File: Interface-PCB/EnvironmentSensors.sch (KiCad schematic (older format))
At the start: 10 parts, among them J10 LEVEL_SENSOR, J11 LEVEL_SENSOR, J12 LEVEL_SENSOR, J13 TEMPERATURE_SENSOR, J14 TEMPERATURE_SENSOR, J7 LEVEL_SENSOR, J8 LEVEL_SENSOR, J9 LEVEL_SENSOR

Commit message: Assign misc footprints for FDP
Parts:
- R13, R14: footprint (none) -> Resistors:AXIAL-0.3-KIT
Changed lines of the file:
@@
 F 0 "R13" H 9220 5546 50  0000 L CNN
 F 1 "4.7k" H 9220 5455 50  0000 L CNN
-F 2 "" V 9080 5500 50  0001 C CNN
+F 2 "Resistors:AXIAL-0.3-KIT" V 9080 5500 50  0001 C CNN
 F 3 "~" H 9150 5500 50  0001 C CNN
 	1    9150 5500
@@
 F 0 "R14" H 9180 4446 50  0000 R CNN
 F 1 "10k" H 9180 4355 50  0000 R CNN
-F 2 "" V 9180 4400 50  0001 C CNN
+F 2 "Resistors:AXIAL-0.3-KIT" V 9180 4400 50  0001 C CNN
 F 3 "~" H 9250 4400 50  0001 C CNN
 	1    9250 4400

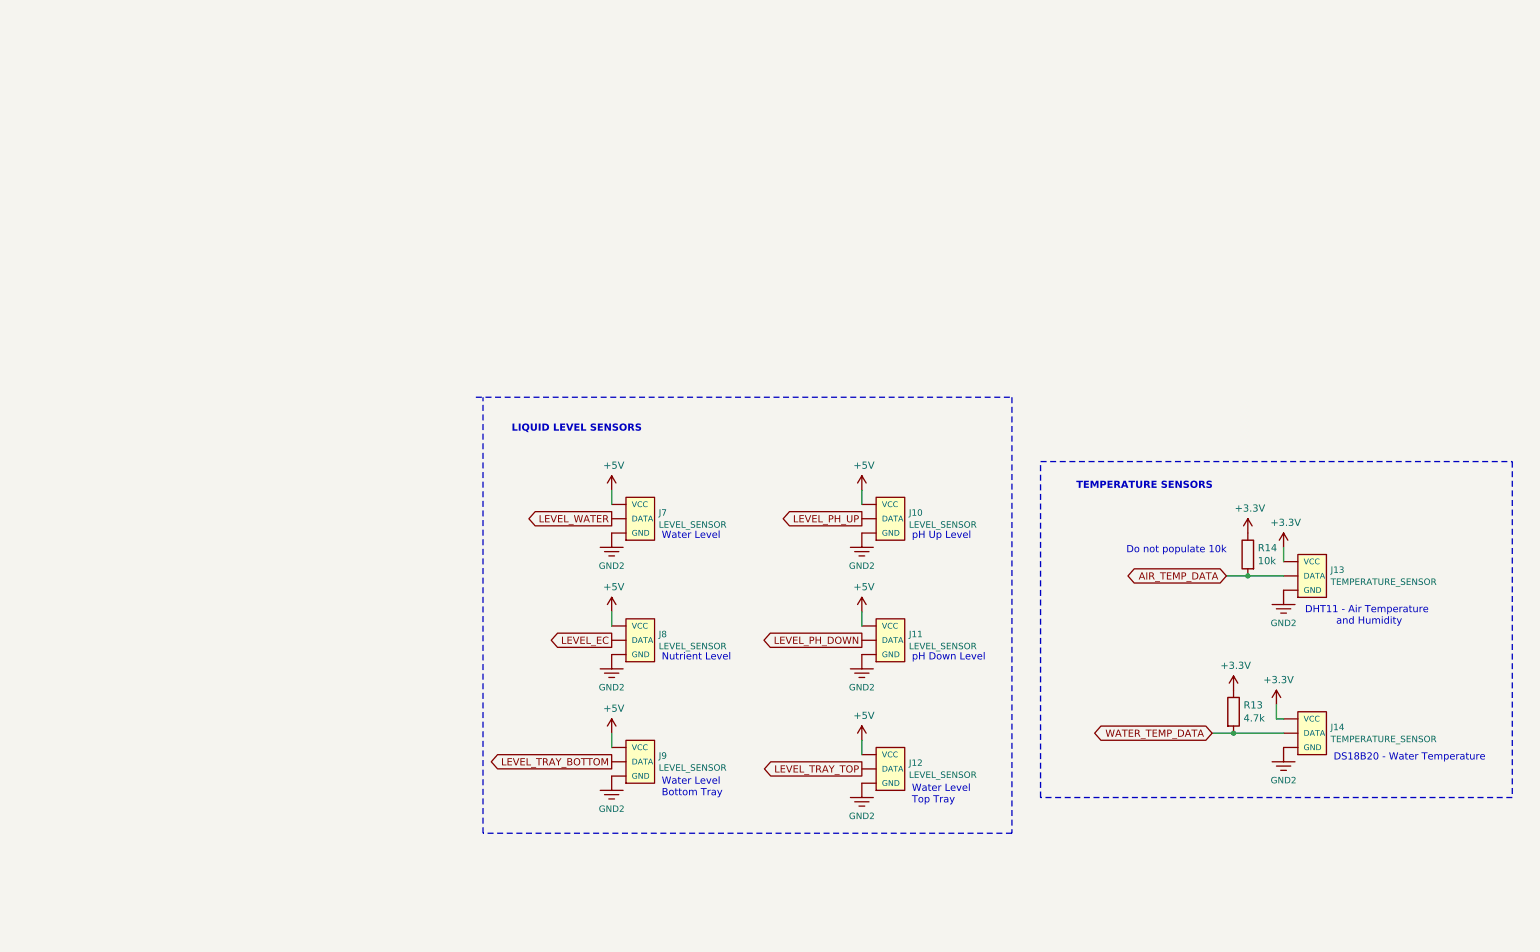
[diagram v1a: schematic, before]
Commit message: Add diagrams and datasheets
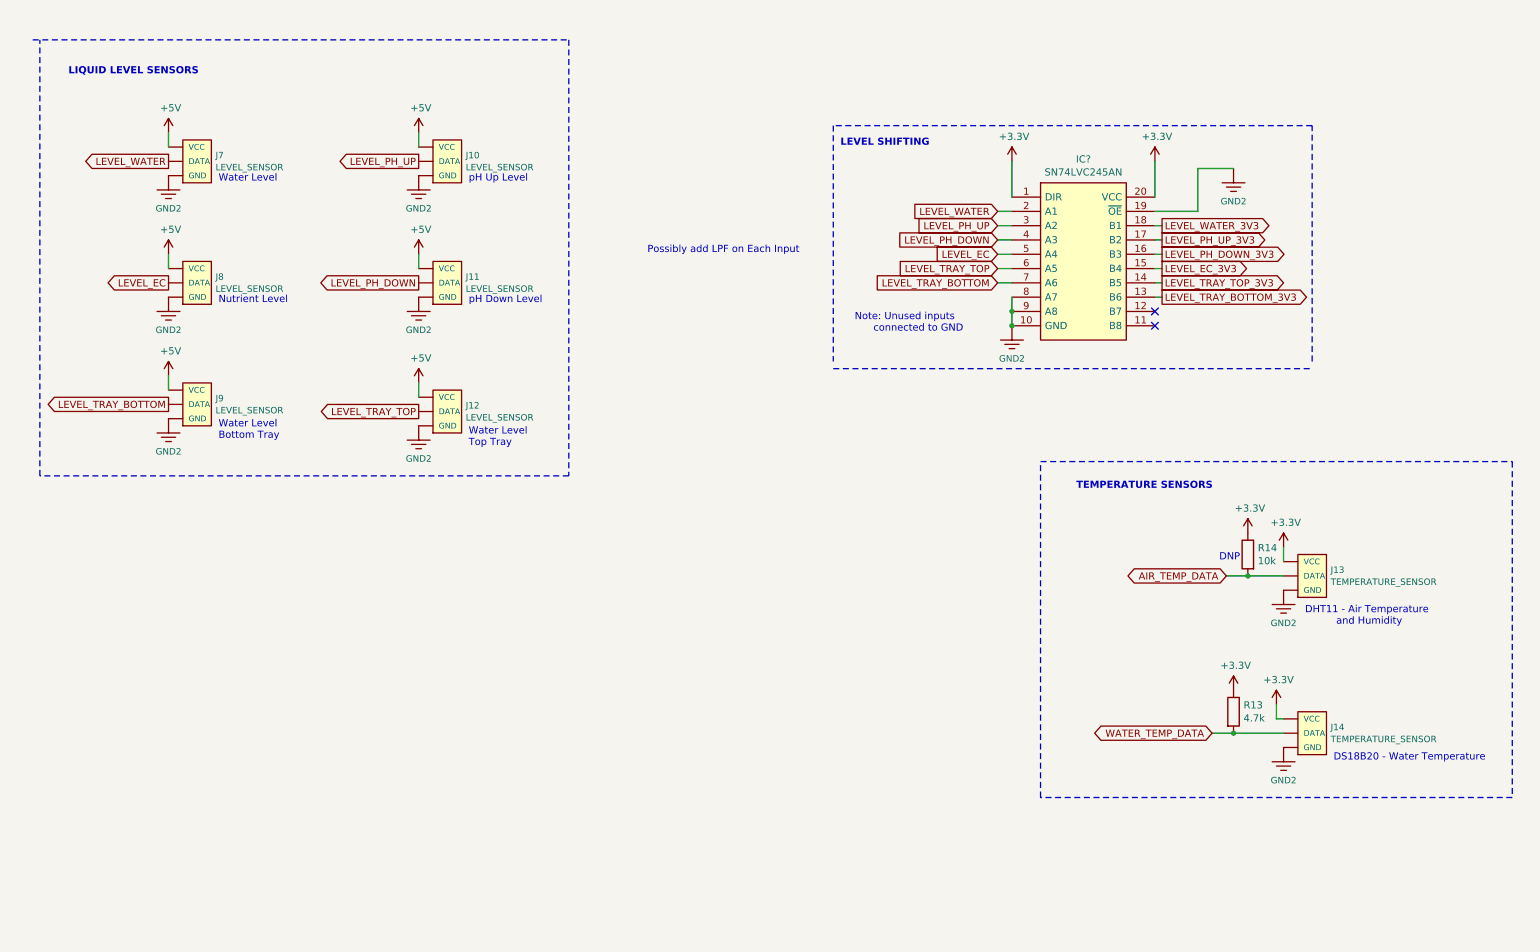
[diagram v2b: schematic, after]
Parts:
- added IC?: SN74LVC245AN, Package_DIP:DIP-20_W7.62mm_LongPads, symbol AA_Custom_Components:SN74LVC245AN
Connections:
- net +3V3: now also IC?.1 (DIR), IC?.20 (VCC)
- net 3.3V: now also IC?.10 (GND), IC?.19 (~OE), IC?.8 (A7), IC?.9 (A8)
- net LEVEL_EC: now also IC?.5 (A4)
- net LEVEL_PH_DOWN: now also IC?.4 (A3)
- net LEVEL_PH_UP: now also IC?.3 (A2)
- net LEVEL_TRAY_BOTTOM: now also IC?.7 (A6)
- net LEVEL_TRAY_TOP: now also IC?.6 (A5)
- net LEVEL_WATER: now also IC?.2 (A1)
- new net LEVEL_EC_3V3: IC?.15 (B4)
- new net LEVEL_PH_DOWN_3V3: IC?.16 (B3)
- new net LEVEL_PH_UP_3V3: IC?.17 (B2)
- new net LEVEL_TRAY_BOTTOM_3V3: IC?.13 (B6)
- new net LEVEL_TRAY_TOP_3V3: IC?.14 (B5)
- new net LEVEL_WATER_3V3: IC?.18 (B1)
- no-connect marks 0 -> 2
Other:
- note added: "DNP"
- note added: "LEVEL SHIFTING"
- note added: "Note: Unused inputs\n connected to GND"
- note added: "Possibly add LPF on Each Input"
- note removed: "Do not populate 10k"
- moved on the sheet: J10, J11, J12, J7, J8, J9

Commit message: Review Schematic
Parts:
- added C3: 100nF, Capacitor_THT:C_Disc_D3.4mm_W2.1mm_P2.50mm, symbol Device:C
- gave numbers to parts that had none: 1
- renumbered J9 to J10, J10 to J11, J11 to J12, J12 to J13, J13 to J14, J14 to J15, J7 to J8, J8 to J9, R13 to R7, R14 to R8
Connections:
- net +3V3: now also C3.1
- net 3.3V renamed GND
- net GND: now also C3.2
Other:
- moved on the sheet: J13

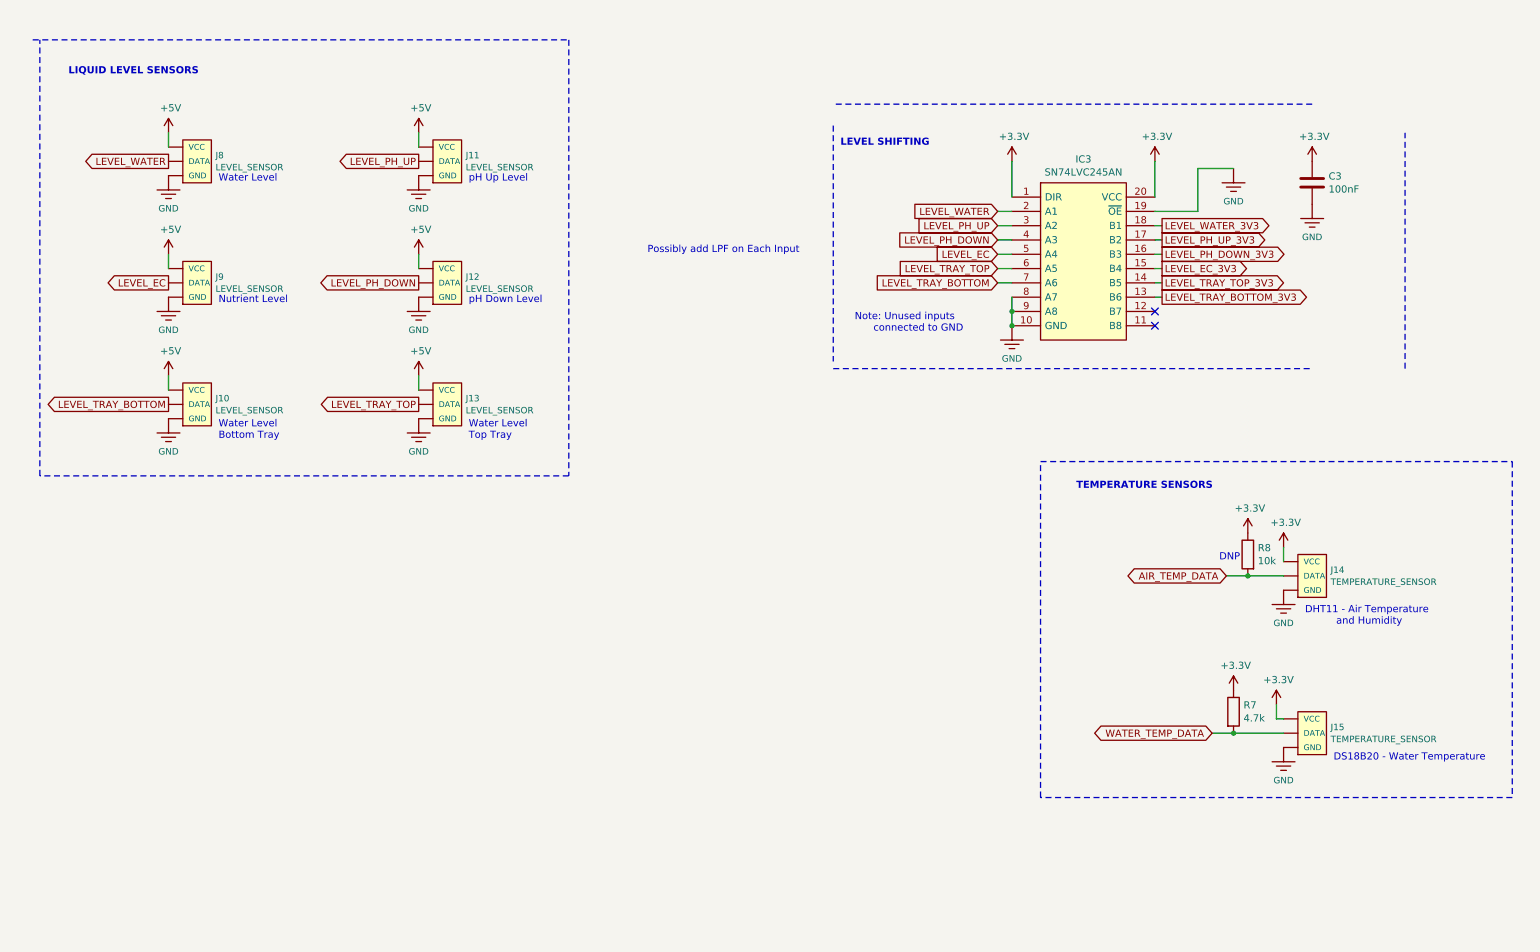
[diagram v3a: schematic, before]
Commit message: Add indicator LEDs
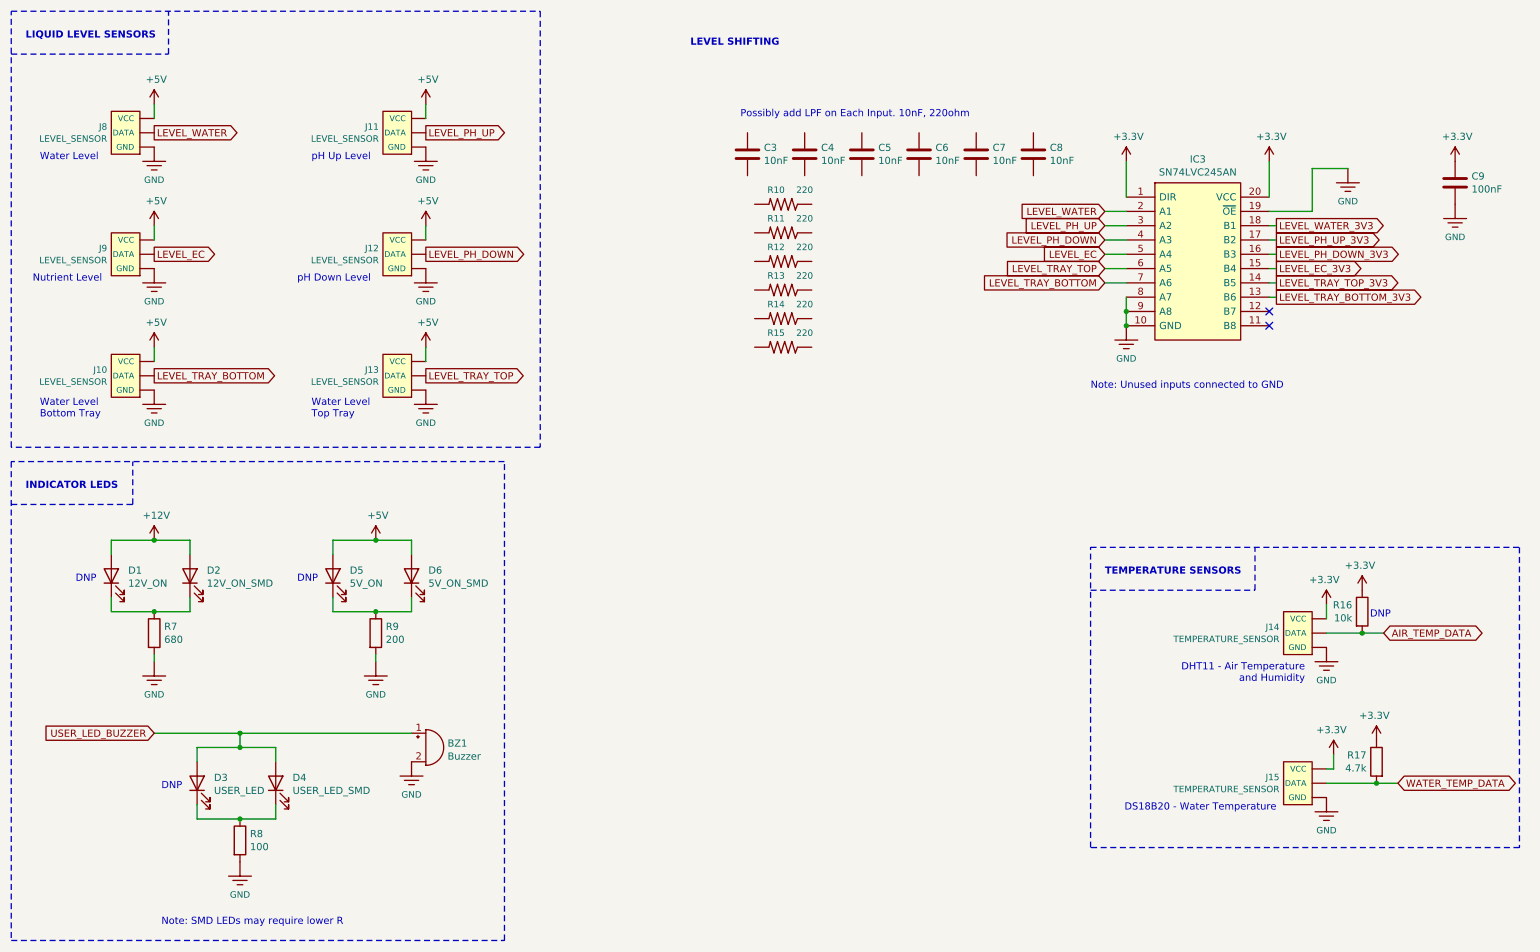
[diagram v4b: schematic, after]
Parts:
- added BZ1: Buzzer, Buzzer_Beeper:Buzzer_TDK_PS1240P02BT_D12.2mm_H6.5mm, symbol Device:Buzzer
- added C3, C4, C5, C6, C7, C8: 10nF, Capacitor_THT:C_Disc_D3.4mm_W2.1mm_P2.50mm, symbol Device:C
- added D1: 12V_ON, LED_THT:LED_D3.0mm, symbol Device:LED
- added D2: 12V_ON_SMD, LED_SMD:LED_1206_3216Metric_Pad1.42x1.75mm_HandSolder, symbol Device:LED
- added D3: USER_LED, LED_THT:LED_D3.0mm, symbol Device:LED
- added D4: USER_LED_SMD, LED_SMD:LED_1206_3216Metric_Pad1.42x1.75mm_HandSolder, symbol Device:LED
- added D5: 5V_ON, LED_THT:LED_D3.0mm, symbol Device:LED
- added D6: 5V_ON_SMD, LED_SMD:LED_1206_3216Metric_Pad1.42x1.75mm_HandSolder, symbol Device:LED
- added R10, R11, R12, R13, R14, R15: 220, Resistor_THT:R_Axial_DIN0207_L6.3mm_D2.5mm_P10.16mm_Horizontal, symbol AA_Custom_Components:R
- added R7: 680, Resistors:AXIAL-0.3-KIT, symbol Device:R
- added R8: 100, Resistors:AXIAL-0.3-KIT, symbol Device:R
- added R9: 200, Resistors:AXIAL-0.3-KIT, symbol Device:R
- renumbered C3 to C9, R8 to R16, R7 to R17
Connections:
- net +5V: now also D5.2 (A), D6.2 (A)
- net GND: now also BZ1.2 (+), R7.2, R8.2, R9.2
- new net: D1.1 (K), D2.1 (K), R7.1
- new net: D5.1 (K), D6.1 (K), R9.1
- new net: D3.1 (K), D4.1 (K), R8.1
- new net +12V: D1.2 (A), D2.2 (A)
- new net USER_LED_BUZZER: BZ1.1 (-), D3.2 (A), D4.2 (A)
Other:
- note added: "INDICATOR LEDS"
- note added: "Note: SMD LEDs may require lower R"
- note added: "Note: Unused inputs connected to GND"
- note added: "Possibly add LPF on Each Input. 10nF, 220ohm"
- note removed: "Note: Unused inputs\n connected to GND"
- note removed: "Possibly add LPF on Each Input"
- moved on the sheet: C9, IC3, J10, J11, J12, J13, J14, J15, J8, J9, R16, R17
